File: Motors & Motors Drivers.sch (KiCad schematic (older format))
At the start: 5 parts, among them J2 Conn_01x02, J3 Conn_01x02, U4 DRV8835

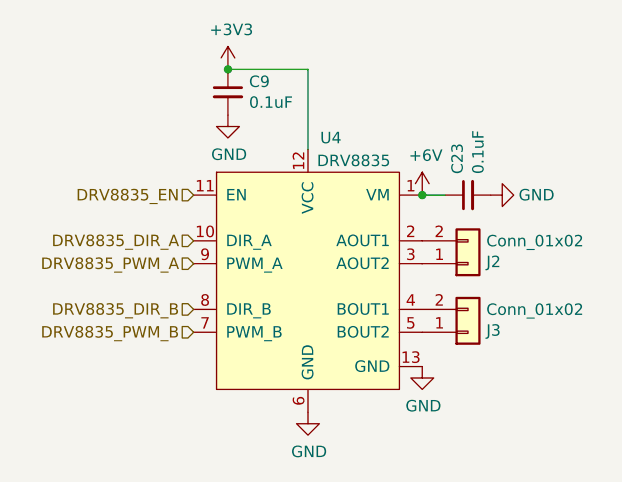
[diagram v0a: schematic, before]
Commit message: Updated BT module connection, 3D models and wiring.
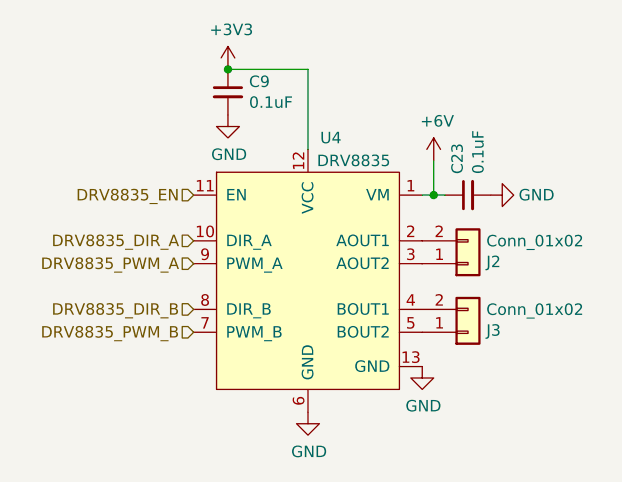
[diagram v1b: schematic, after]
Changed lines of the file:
@@
 L power:+6V #PWR0119
 U 1 1 5E6FE882
-P 6200 2900
-F 0 "#PWR0119" H 6200 2750 50  0001 C CNN
-F 1 "+6V" H 6215 3073 50  0000 C CNN
-F 2 "" H 6200 2900 50  0001 C CNN
-F 3 "" H 6200 2900 50  0001 C CNN
-	1    6200 2900
+P 6250 2750
+F 0 "#PWR0119" H 6250 2600 50  0001 C CNN
+F 1 "+6V" H 6265 2923 50  0000 C CNN
+F 2 "" H 6250 2750 50  0001 C CNN
+F 3 "" H 6250 2750 50  0001 C CNN
+	1    6250 2750
 	1    0    0    -1
 $EndComp
@@
 $EndComp
 Wire Wire Line
-	6300 2900 6200 2900
-Connection ~ 6200 2900
+	6300 2900 6250 2900
+Wire Wire Line
+	6250 2750 6250 2900
+Connection ~ 6250 2900
+Wire Wire Line
+	6250 2900 6200 2900
 $EndSCHEMATC
